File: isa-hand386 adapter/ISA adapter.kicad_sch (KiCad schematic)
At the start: 13 parts, among them J1 Conn_02x30_Odd_Even, J2 Conn_02x30_Odd_Even, J3 Bus_ISA_8bit, J4 IRQDMA_JP, J5 Wavetable, J6 AudioJack3

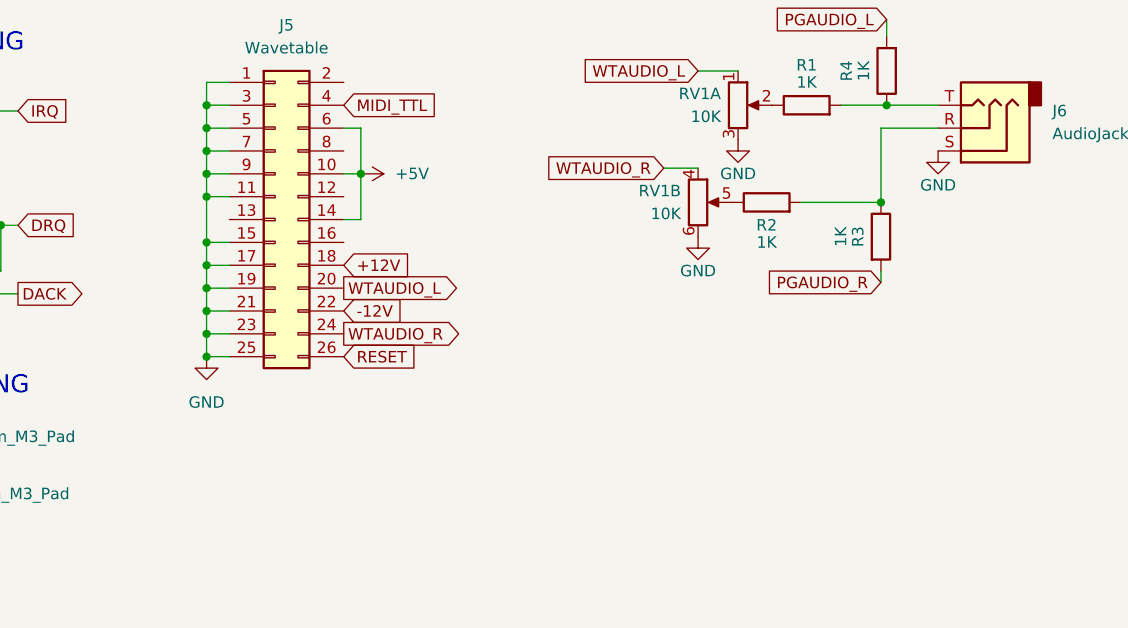
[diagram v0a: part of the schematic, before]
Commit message: Prototype ISA adapter produced on 2023-07-01
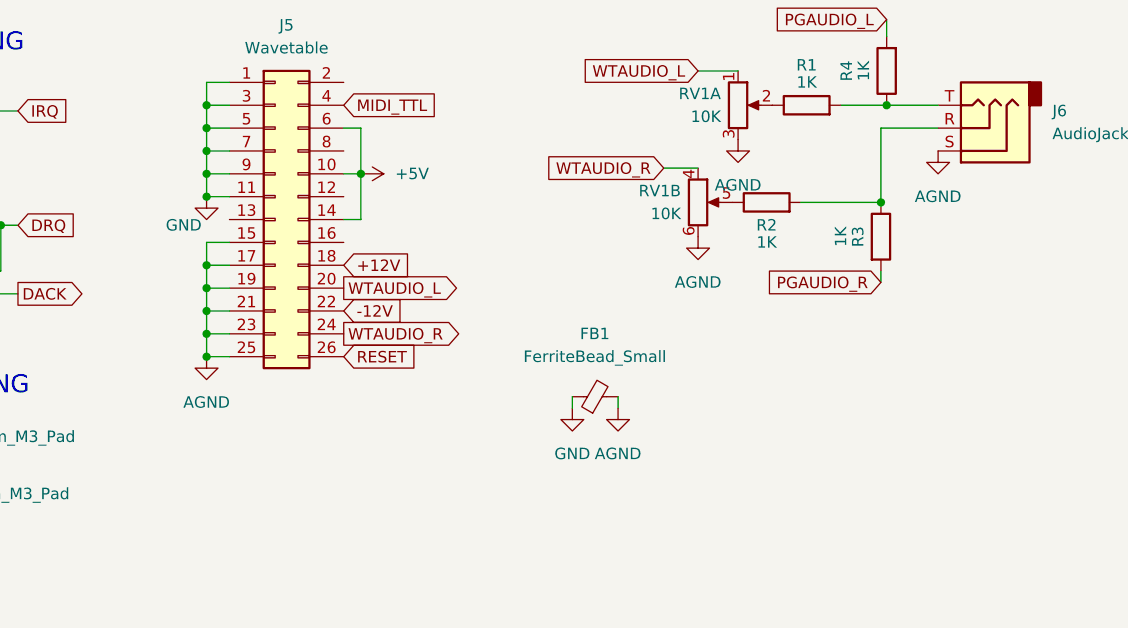
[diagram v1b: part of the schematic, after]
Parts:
- added FB1: FerriteBead_Small, Inductor_SMD:L_0805_2012Metric, symbol Device:FerriteBead_Small
- R1, R2, R3, R4: footprint Resistor_THT:R_Axial_DIN0207_L6.3mm_D2.5mm_P7.62mm_Horizontal -> Resistor_SMD:R_0805_2012Metric
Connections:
- net GND: now also FB1.1; no longer J5.15 (Pin_15), J5.17 (Pin_17), J5.19 (Pin_19), J5.21 (Pin_21), J5.23 (Pin_23), J5.25 (Pin_25), J6.S, RV1.3, RV1.6
- new net GNDS: FB1.2, J5.15 (Pin_15), J5.17 (Pin_17), J5.19 (Pin_19), J5.21 (Pin_21), J5.23 (Pin_23), J5.25 (Pin_25), J6.S, RV1.3, RV1.6

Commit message: ISA adapter v1.1/Hand386 PicoGUS v1.0
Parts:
- removed J6: AudioJack3, Connector_Audio:Jack_3.5mm_CUI_SJ1-3533NG_Horizontal, symbol Connector_Audio:AudioJack3
- added C1: 100nF, Capacitor_SMD:C_0805_2012Metric, symbol Device:C
- added J6: AudioJack3, Connector_Audio:Jack_3.5mm_CUI_SJ1-3535NG_Horizontal, symbol Connector_Audio:AudioJack3_SwitchTR
- added U1: 74HC14, Package_SO:SOIC-14_3.9x8.7mm_P1.27mm, symbol 74xx:74HC14
- H1, H2: footprint MountingHole:MountingHole_3.2mm_M3_Pad -> MountingHole:MountingHole_3.2mm_M3_ISO14580_Pad
- RV1: footprint PiGUS library:PTD9022015FB102 -> PiGUS library:RK10J12R0A0B
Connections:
- net +5V: now also C1.1, U1.11, U1.13, U1.14 (VCC), U1.9
- net GND: now also C1.2, U1.7 (GND)
- net GNDS: now also J6.S
- net RESET: now also U1.1; no longer J5.26 (Pin_26)
- net WTAUDIO_L: now also J5.24 (Pin_24); no longer J5.20 (Pin_20)
- net WTAUDIO_R: now also J5.20 (Pin_20); no longer J5.24 (Pin_24)
- net at R1.2, R4.1: now also J6.T
- net at R2.2, R3.1: now also J6.R
- new net: U1.2, U1.3
- new net: U1.4, U1.5
- new net ~{RESET}: J5.26 (Pin_26), U1.6
- no-connect marks 0 -> 75
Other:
- title: PicoGUS v1.1 -> Micro-PicoGUS ISA adapter v1.1
- moved on the sheet: FB1

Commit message: Hand386 version and ISA adapter fabbed at JLC 8/25
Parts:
- removed J2: Conn_02x30_Odd_Even, PiGUS library:Hand386_PicoGUS, symbol Connector_Generic:Conn_02x30_Odd_Even
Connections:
- no-connect marks 75 -> 50

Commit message: Updates to femto & ISA adapter for mid-2024 batch
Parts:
- removed FB1: FerriteBead_Small, Inductor_SMD:L_0805_2012Metric, symbol Device:FerriteBead_Small
- added NT1: NetTie_2, NetTie:NetTie-2_SMD_Pad2.0mm, symbol Device:NetTie_2
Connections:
- net GND: now also NT1.1
- net GNDS: now also NT1.2
